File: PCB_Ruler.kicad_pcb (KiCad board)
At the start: 2 copper layers, 100.5 x 27 mm, 92 parts, among them Q1 SOT23-3, Q10 SOT89, Q11 SOT886, Q12 SOT963, Q13 SSOP-16, Q14 SSOP-8, Q15 SOT1113, Q16 SOT665, Q2 SOT23-5, Q3 SOT323, Q4 SOT353, Q5 SOT553, Q6 DPAK, Q7 DP2AK, Q8 LFPAK, Q9 SOT223, U1 1.00, U10 5mm, U11 6mm, U12 7mm, U13 8mm, U14 9mm, U15 3_10in, U16 0_16in, U17 1_16in, U18 2_16in, U19 3_16in, U2 1.27, U20 0_10in, U21 1_10in, U22 2_10in, U3 2.00, U4 2.54, U5 0mm, U6 1mm, U7 2mm, U8 3mm, U9 4mm

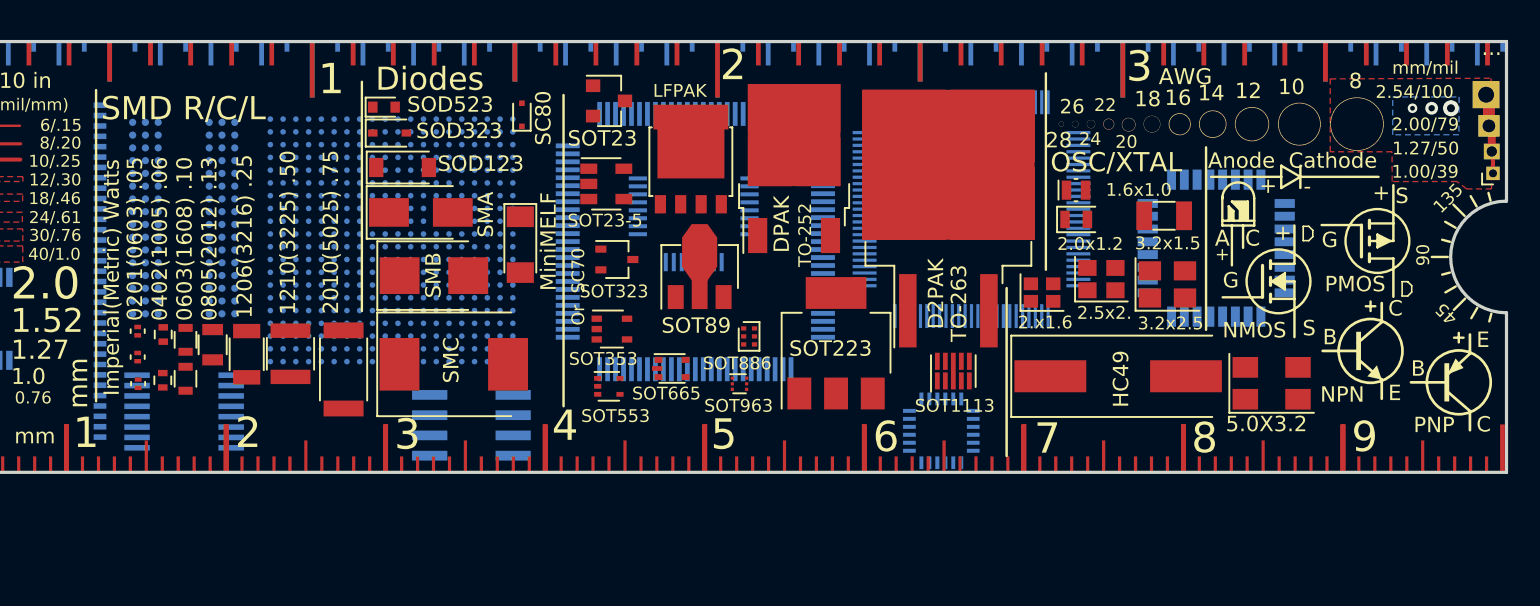
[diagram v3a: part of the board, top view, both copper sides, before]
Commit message: Starting on back side, now all pin 1s are connected
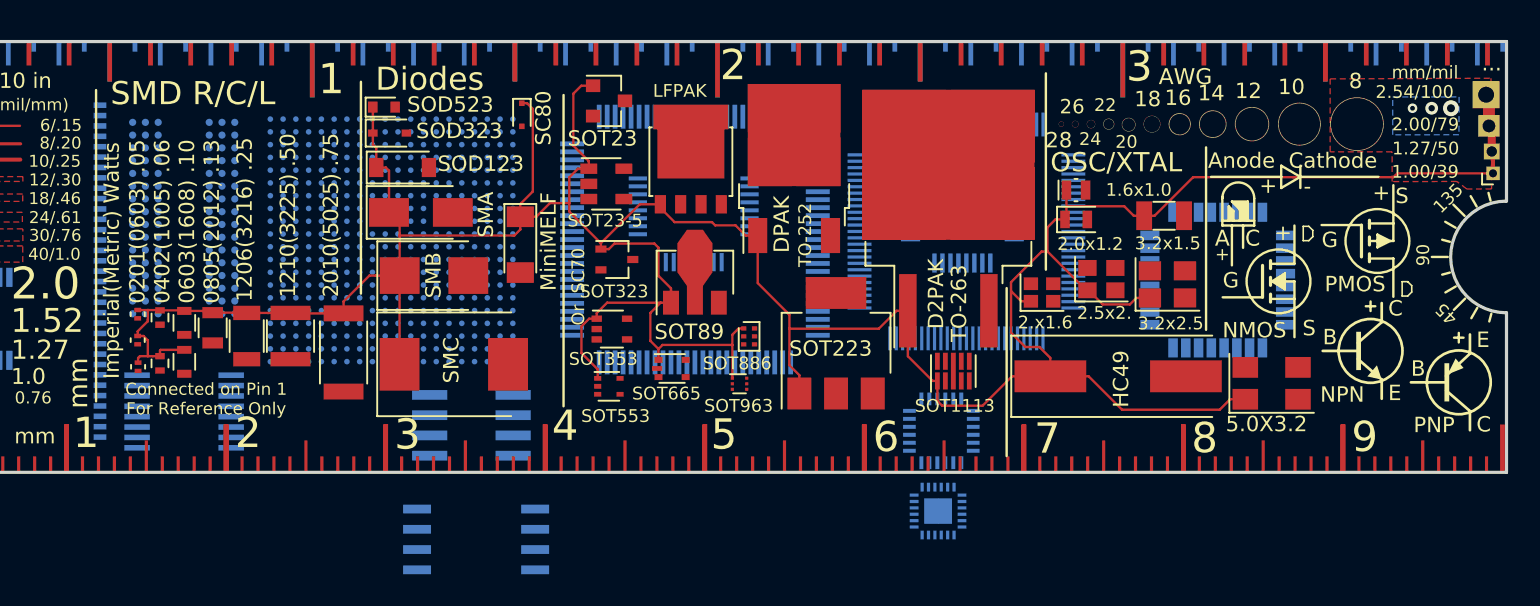
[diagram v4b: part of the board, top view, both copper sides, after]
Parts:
- removed E$65: , Adafruit PCB Reference Ruler:TQFP100
- removed E$68: , Adafruit PCB Reference Ruler:TQFP-100-12X12MM
- removed E$69: , Adafruit PCB Reference Ruler:TQFP32-08
- added Q17: SO-8, Housings_SOIC:SO-8_5.3x6.2mm_Pitch1.27mm, B.Cu at (105.9, 124.2)
- added Q18: QFNx24, Housings_DFN_QFN:QFN-24-1EP_3x3mm_Pitch0.4mm, B.Cu at (134.9, 122.4)
- added Q19: QFPx100_0.5, Housings_QFP:TQFP-100_14x14mm_Pitch0.5mm, B.Cu at (119.6, 105.4)
- added Q20: QFPx32, Housings_QFP:LQFP-32_5x5mm_Pitch0.5mm, B.Cu at (136.4, 103.6)
- added Q21: QFPx32_0.8, Housings_QFP:LQFP-32_7x7mm_Pitch0.8mm, B.Cu at (152.4, 108.0)
- added Q22: QFPx100, Housings_QFP:TQFP-100_12x12mm_Pitch0.4mm, B.Cu at (136.7, 104.9)
- moved R9 1.14 mm to (91.5, 111.5), turned to 270 degrees
- moved R10 1.11 mm to (94.3, 111.5), turned to 270 degrees
- moved R5 1.08 mm to (86.1, 110.3), turned to 270 degrees
- moved R4 1.08 mm to (86.1, 113.2), turned to 270 degrees
- moved R7 1.06 mm to (87.6, 110.6), turned to 270 degrees
- moved R6 1.06 mm to (87.6, 113.1), turned to 270 degrees
- moved R1 1.06 mm to (84.7, 110.1), turned to 270 degrees
- moved R11 1.06 mm to (97.6, 112.5), turned to 270 degrees
- moved R2 1.06 mm to (84.7, 111.7), turned to 270 degrees
- moved R3 1.06 mm to (84.7, 113.4), turned to 270 degrees
- moved R8 1.06 mm to (89.4, 110.9), turned to 270 degrees
- moved Q10 0.46 mm to (119.6, 107.9)
- turned D1 to 270 degrees
- turned XT8 to 180 degrees
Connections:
- D1 pad 1: (no net) -> /Pin1
- D2 pad 1: (no net) -> /Pin1
- D3 pad 1: (no net) -> /Pin1
- D4 pad 1: (no net) -> /Pin1
- D5 pad 1: (no net) -> /Pin1
- D6 pad 1: (no net) -> /Pin1
- D7 pad 1: (no net) -> /Pin1
- D8 pad 1: (no net) -> /Pin1
- Q1 pad 1: (no net) -> /Pin1
- Q10 pad 1: (no net) -> /Pin1
- Q11 pad 1: (no net) -> /Pin1
- Q12 pad 1: (no net) -> /Pin1
- Q15 pad 1: (no net) -> /Pin1
- Q16 pad 1: (no net) -> /Pin1
- Q2 pad 1: (no net) -> /Pin1
- Q3 pad 1: (no net) -> /Pin1
- Q4 pad 1: (no net) -> /Pin1
- Q5 pad 1: (no net) -> /Pin1
- Q6 pad 1: (no net) -> /Pin1
- Q7 pad 1: (no net) -> /Pin1
- Q8 pad 1: (no net) -> /Pin1
- Q9 pad 1: (no net) -> /Pin1
- R1 pad 1: (no net) -> /Pin1
- R10 pad 1: (no net) -> /Pin1
- R11 pad 1: (no net) -> /Pin1
- R2 pad 1: (no net) -> /Pin1
- R3 pad 1: (no net) -> /Pin1
- R4 pad 1: (no net) -> /Pin1
- R5 pad 1: (no net) -> /Pin1
- R6 pad 1: (no net) -> /Pin1
- R7 pad 1: (no net) -> /Pin1
- R8 pad 1: (no net) -> /Pin1
- R9 pad 1: (no net) -> /Pin1
- U1 pad 1: /Via -> /Pin1
- U2 pad 1: /Via -> /Pin1
- U3 pad 1: /Via -> /Pin1
- U4 pad 1: /Via -> /Pin1
- XT1 pad 1: (no net) -> /Pin1
- XT2 pad 1: (no net) -> /Pin1
- XT3 pad 1: (no net) -> /Pin1
- XT4 pad 1: (no net) -> /Pin1
- XT5 pad 1: (no net) -> /Pin1
- XT6 pad 1: (no net) -> /Pin1
- XT7 pad 1: (no net) -> /Pin1
- XT8 pad 1: (no net) -> /Pin1
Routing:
- net /Pin1: track 0.00 -> 222.8 mm, vias 0 -> 3
- net /Via: track 5.36 -> 0.00 mm, vias 3 -> 0
- added copper zone on F.Cu, net /Pin1
- removed copper zone on F.Cu, net /Via
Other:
- rule trace_min: 0.2 -> 0.15
- board text added: "Connected on Pin 1 For Reference Only"
- board text added: "Modified Adafruit PCB Ruler v2 For Reference Only M Young"
- board text removed: "Modified Adafruit PCB Ruler v1 M Young"

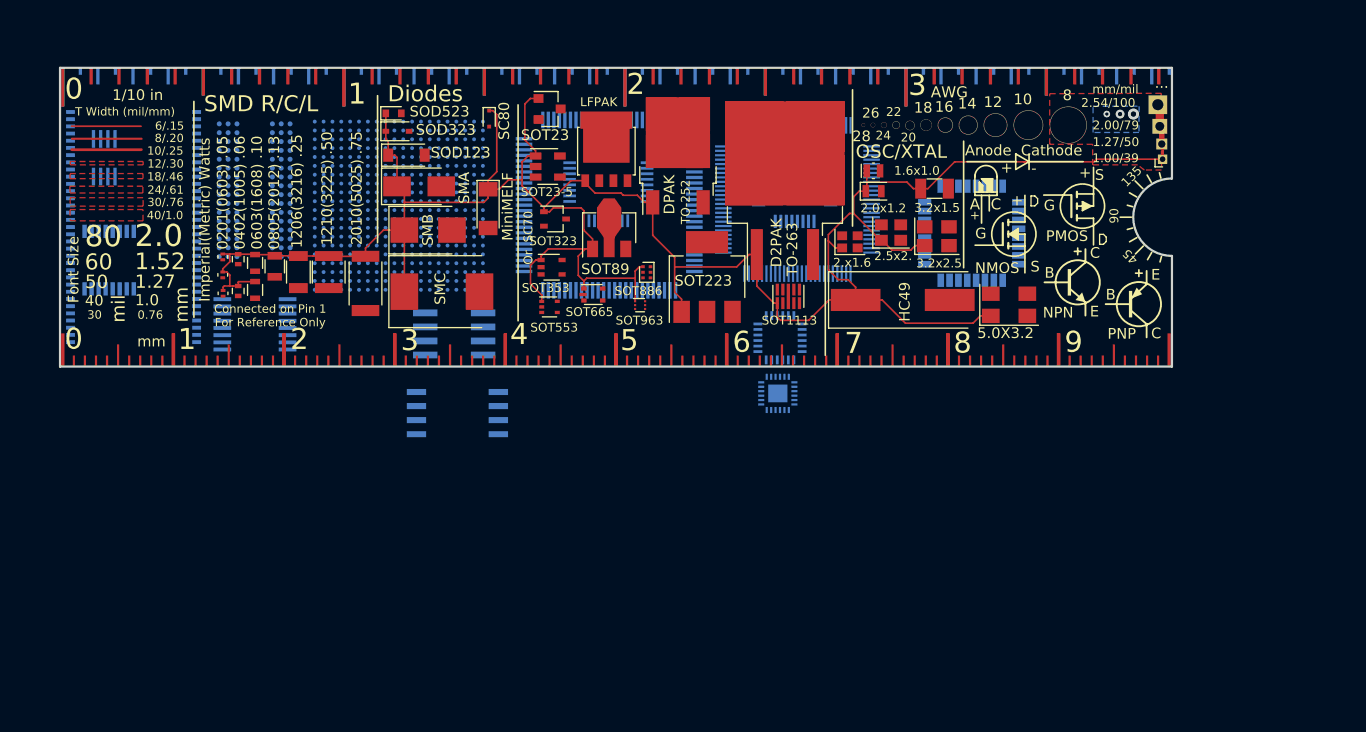
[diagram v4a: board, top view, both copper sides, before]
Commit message: Added more QF{P/N} to bottom
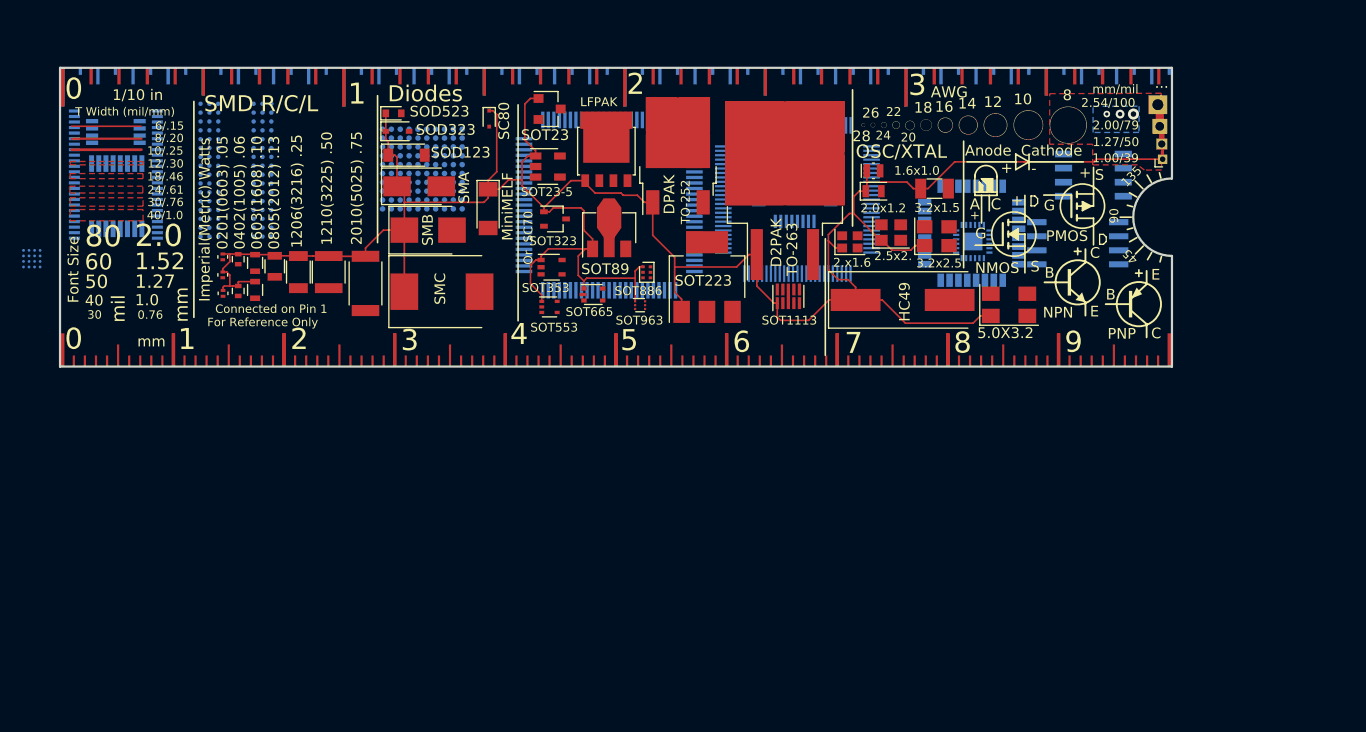
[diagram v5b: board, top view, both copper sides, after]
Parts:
- removed E$55: , Adafruit PCB Reference Ruler:QFN-24
- removed E$56: , Adafruit PCB Reference Ruler:TSSOP16
- removed E$57: , Adafruit PCB Reference Ruler:SO08
- removed E$66: , Adafruit PCB Reference Ruler:TSOP-66
- removed E$67: , Adafruit PCB Reference Ruler:BGA-0.8MM-P-19X19
- removed E$70: , Adafruit PCB Reference Ruler:TQFP32-5MM
- removed E$71: , Adafruit PCB Reference Ruler:BGA-96-14X8MM
- added Q23: SOIC, Housings_SOIC:SOIC-8_3.9x4.9mm_Pitch1.27mm, B.Cu at (163.4, 102.7)
- added Q24: TSOP-48, Housings_SSOP:TSSOP-48_6.1x12.5mm_Pitch0.5mm, B.Cu at (75.0, 102.7)
- added Q25: BGA_DDR3, Housings_BGA:BGA-96_2x3x16_9.0x13.0mm_Pitch0.8mm, B.Cu at (85.9, 102.2)
- added Q26: BGA_10x, Housings_BGA:BGA-100_10x10_9.0x9.0mm_Pitch0.8mm, B.Cu at (102.8, 102.2)
- added Q27: BGA_4x, Housings_BGA:BGA-16_4x4_1.92x1.92mm_Pitch0.5mm, B.Cu at (67.5, 110.2)
- Q13: footprint Housings_SSOP:SSOP-16_3.9x4.9mm_Pitch0.635mm -> Housings_SSOP:TSSOP-16_4.4x5mm_Pitch0.65mm
- Q14: footprint Housings_SSOP:SSOP-8_2.95x2.8mm_Pitch0.65mm -> Housings_SSOP:TSSOP-8_3x3mm_Pitch0.65mm
- moved Q17 58.1 mm to (162.0, 108.9), turned to 180 degrees
- moved Q18 22.3 mm to (152.5, 108.7), turned to 180 degrees
- moved Q13 5.82 mm to (75.1, 104.6)
- moved Q14 2.56 mm to (75.0, 98.8), turned to 180 degrees
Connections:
- Q13 pad 1: (no net) -> /Pin1
- Q14 pad 1: (no net) -> /Pin1
- Q17 pad 1: (no net) -> /Pin1
- Q18 pad 1: (no net) -> /Pin1
- Q19 pad 1: (no net) -> /Pin1
- Q20 pad 1: (no net) -> /Pin1
- Q21 pad 1: (no net) -> /Pin1
- Q22 pad 1: (no net) -> /Pin1
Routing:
- added copper zone on B.Cu, net /Pin1
- removed copper zone on B.Cu, net /Via
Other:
- board text added: "Connected on Pin 1"
- board text added: "For Reference Only"
- board text added: "For Reference Only P = Pitch (mm)"
- board text added: "Modified Adafruit PCB Ruler v2 M Young"
- board text added: "SO-8 P1.27"
- board text added: "SOIC -8"
- board text added: "SSOP -8"
- board text added: "SSOP-8 P0.65"
- board text added: "TSSOP-48 P0.5"
- board text removed: "0.65mm Pitch"
- board text removed: "0.8mm Pitch"
- board text removed: "Connected on Pin 1 For Reference Only"
- board text removed: "Modified Adafruit PCB Ruler v2 For Reference Only M Young"
- board text removed: "QFP x32"
- board text removed: "SOIC"
- board text removed: "SSOP"
- board text removed: "SSOP -16"
- board text removed: "SSOP-8"
- board text removed: "TSOP-66 0.65mm Pitch"

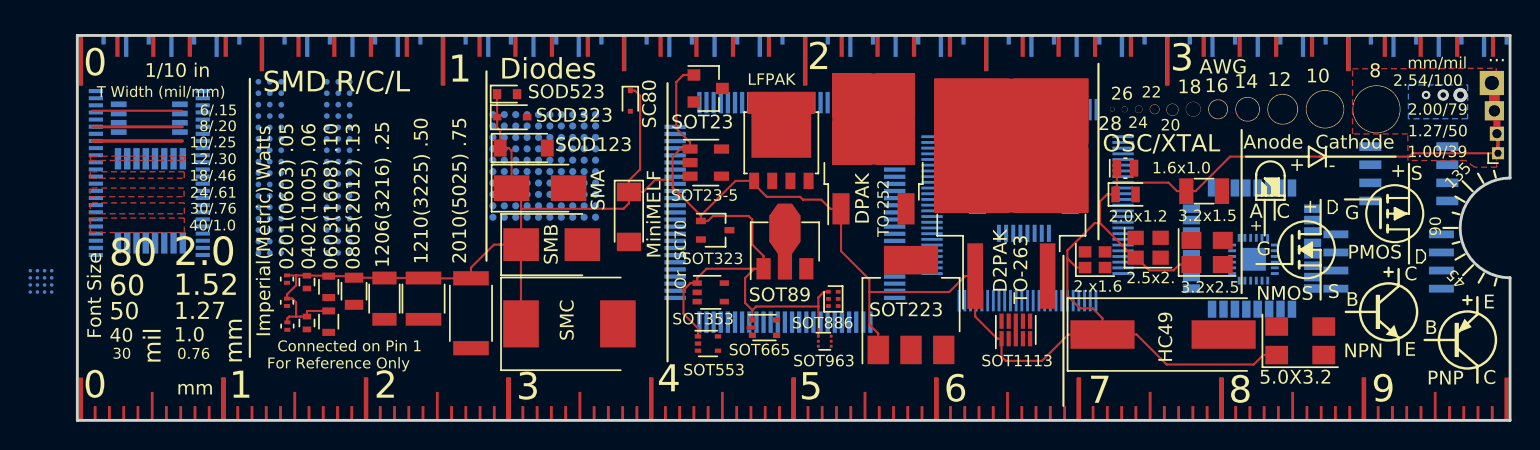
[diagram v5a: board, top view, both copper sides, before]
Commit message: Edited back, added more QF* parts
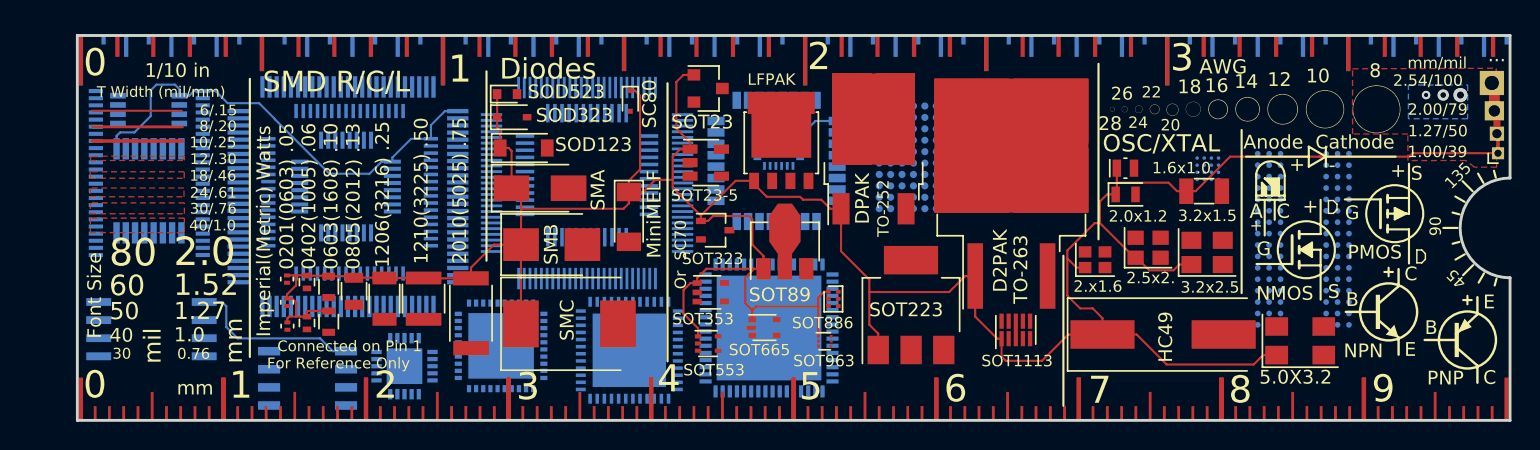
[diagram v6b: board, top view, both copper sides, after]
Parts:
- added Q28: QNFx20, Housings_DFN_QFN:QFN-20-1EP_4x4mm_Pitch0.5mm, B.Cu at (93.0, 116.2)
- added Q29: QNFx40, Housings_DFN_QFN:QFN-40-1EP_6x6mm_Pitch0.5mm, B.Cu at (99.7, 114.8)
- added Q30: QNFx48, Housings_DFN_QFN:QFN-48-1EP_7x7mm_Pitch0.5mm, B.Cu at (108.7, 115.1)
- added Q31: QNFx64, Housings_DFN_QFN:QFN-64-1EP_9x9mm_Pitch0.5mm, B.Cu at (118.5, 113.5)
- added Q32: QFPx48, Housings_QFP:LQFP-48_7x7mm_Pitch0.5mm, B.Cu at (105.8, 102.8)
- added Q33: QFPx64, Housings_QFP:LQFP-64_10x10mm_Pitch0.5mm, B.Cu at (89.1, 104.0)
- moved Q17 86.9 mm to (75.2, 113.6)
- moved Q27 82.2 mm to (149.3, 102.3)
- moved Q23 78.6 mm to (86.2, 117.0)
- moved Q25 70.3 mm to (156.0, 107.3)
- moved Q20 47.5 mm to (88.8, 103.6)
- moved Q18 34.3 mm to (119.2, 100.7)
- moved Q21 33.9 mm to (119.0, 101.8)
- moved Q22 30.9 mm to (105.8, 103.4)
- moved Q19 30.7 mm to (89.0, 104.3)
- moved Q26 27.1 mm to (129.8, 101.5)
- moved Q13 0.71 mm to (75.0, 103.9)
- moved Q14 0.60 mm to (75.0, 98.2)
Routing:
- net /Pin1: track 222.8 -> 271.0 mm
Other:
- board text added: "QFN x24 P0.4"
- board text added: "QFN x40 P0.5"
- board text added: "QFN x64 P0.5"
- board text added: "QFP x100 P0.4"
- board text added: "QFP x32 P0.5"
- board text added: "QFP x32 P0.8"
- board text added: "QFP x48 P0.5"
- board text added: "x100"
- board text added: "x20"
- board text added: "x48"
- board text added: "x64"
- board text removed: "QFN"
- board text removed: "QFP x100 0.4mm Pitch"
- board text removed: "QFP x100 0.5mm Pitch"
- board text removed: "QFP x32 0.8mm Pitch"
